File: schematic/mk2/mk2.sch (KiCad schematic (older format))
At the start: 0 parts

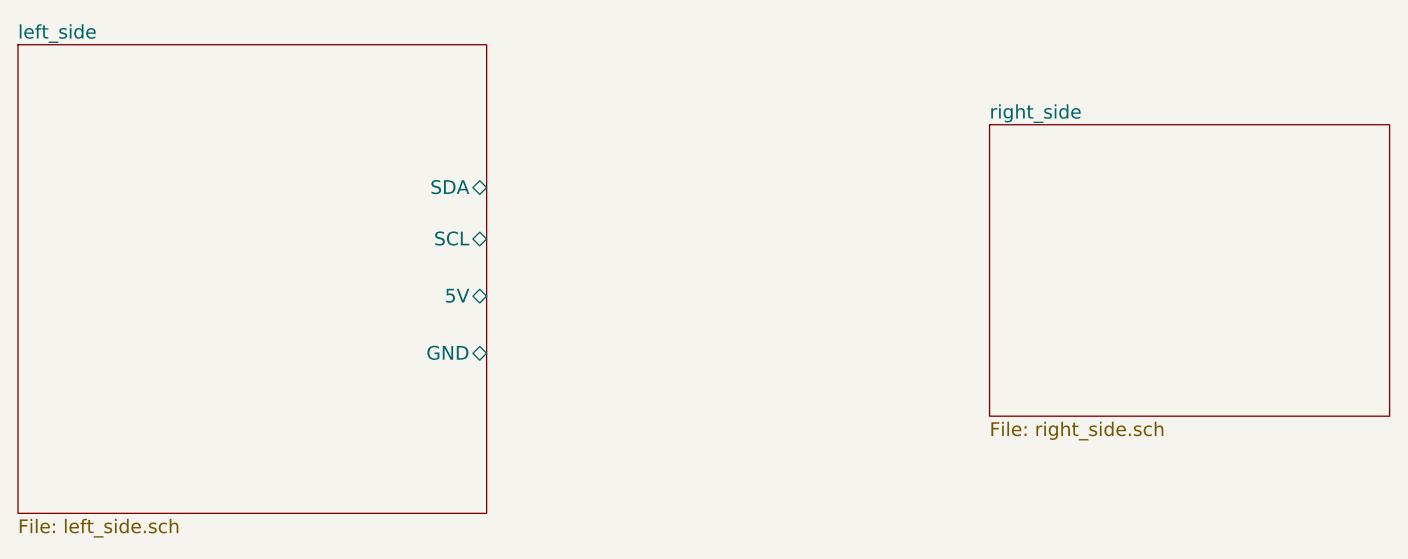
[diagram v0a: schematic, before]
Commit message: schematic: Add the i2c port on the right side and connect left and right sides with wires
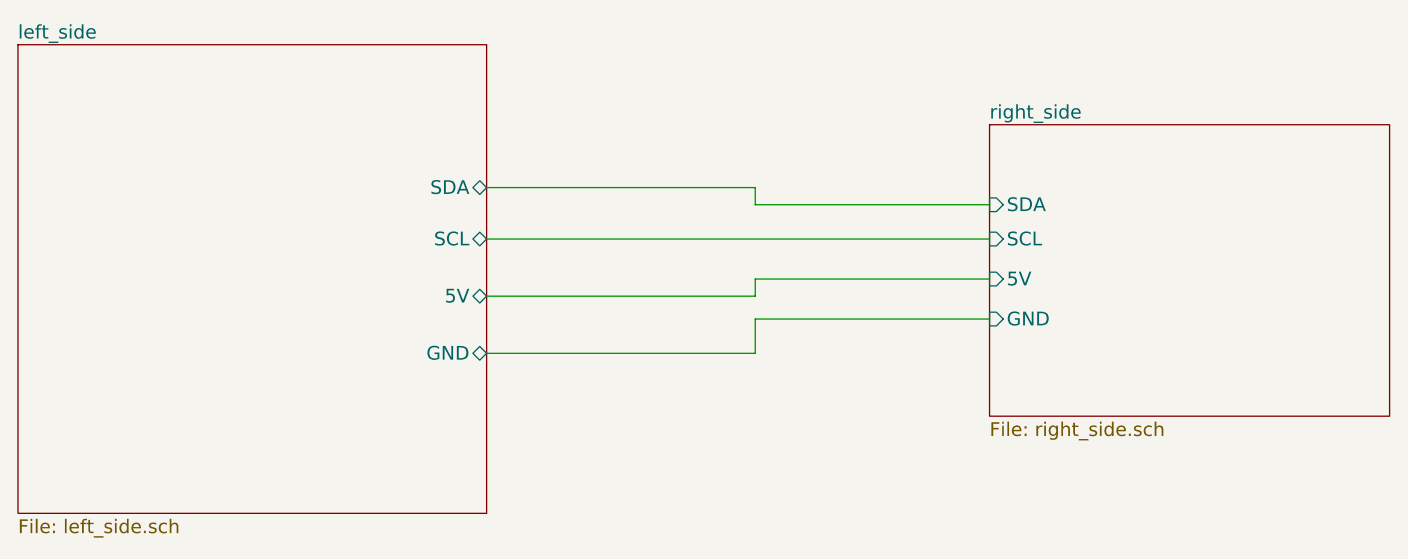
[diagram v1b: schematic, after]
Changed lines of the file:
@@
 F0 "right_side" 60
 F1 "right_side.sch" 60
+F2 "SDA" I L 7275 2700 60
+F3 "SCL" I L 7275 2850 60
+F4 "5V" I L 7275 3025 60
+F5 "GND" I L 7275 3200 60
 $EndSheet
+Wire Wire Line
+	5075 2625 6250 2625
+Wire Wire Line
+	6250 2625 6250 2700
+Wire Wire Line
+	6250 2700 7275 2700
+Wire Wire Line
+	5075 2850 7275 2850
+Wire Wire Line
+	5075 3100 6250 3100
+Wire Wire Line
+	6250 3100 6250 3025
+Wire Wire Line
+	6250 3025 7275 3025
+Wire Wire Line
+	5075 3350 6250 3350
+Wire Wire Line
+	6250 3350 6250 3200
+Wire Wire Line
+	6250 3200 7275 3200
 $EndSCHEMATC
